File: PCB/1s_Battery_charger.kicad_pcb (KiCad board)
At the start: 2 copper layers, 40 x 57 mm, 54 parts, among them J1 Battery connector, J2 USB_C_Receptacle_PowerOnly_6P, J3 Battery connector, J4 Conn_01x04, J5 Battery connector, J6 Conn_01x03, U1 TCA9548APWR, U2 BQ25895RTW, U3 XIAO-ESP32-S3-SMD, U4 BQ25895RTW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

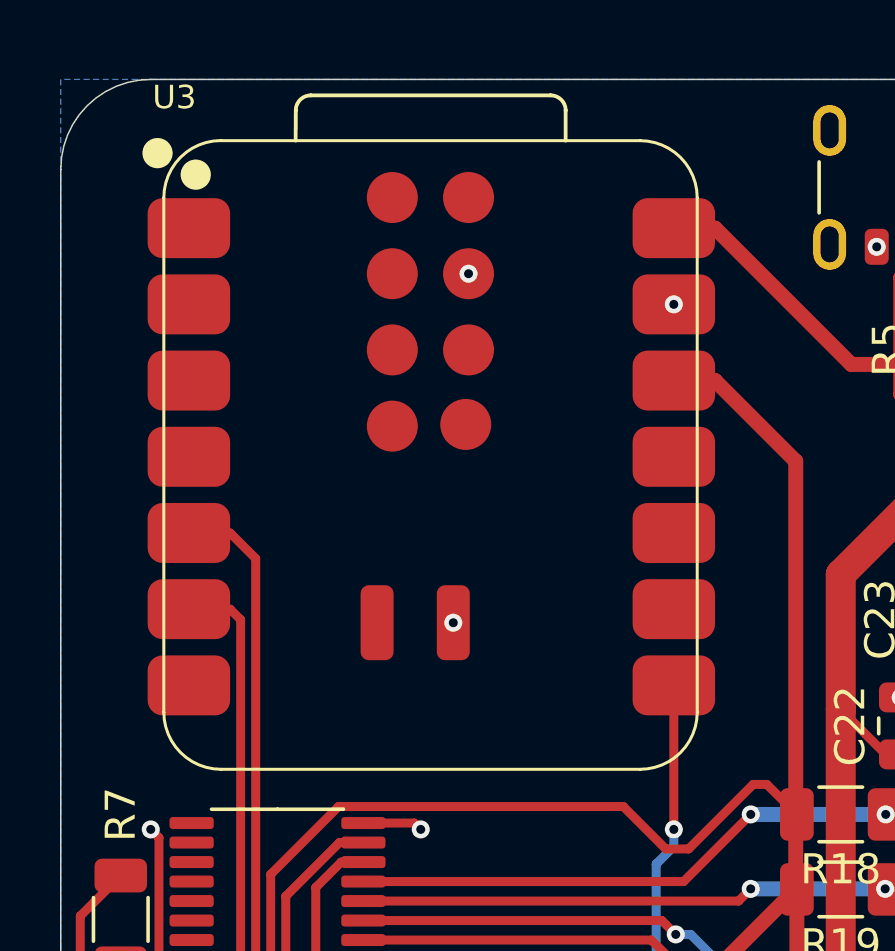
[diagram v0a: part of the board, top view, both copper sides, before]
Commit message: Fixed the issue with XIAO module being too far from the board edge
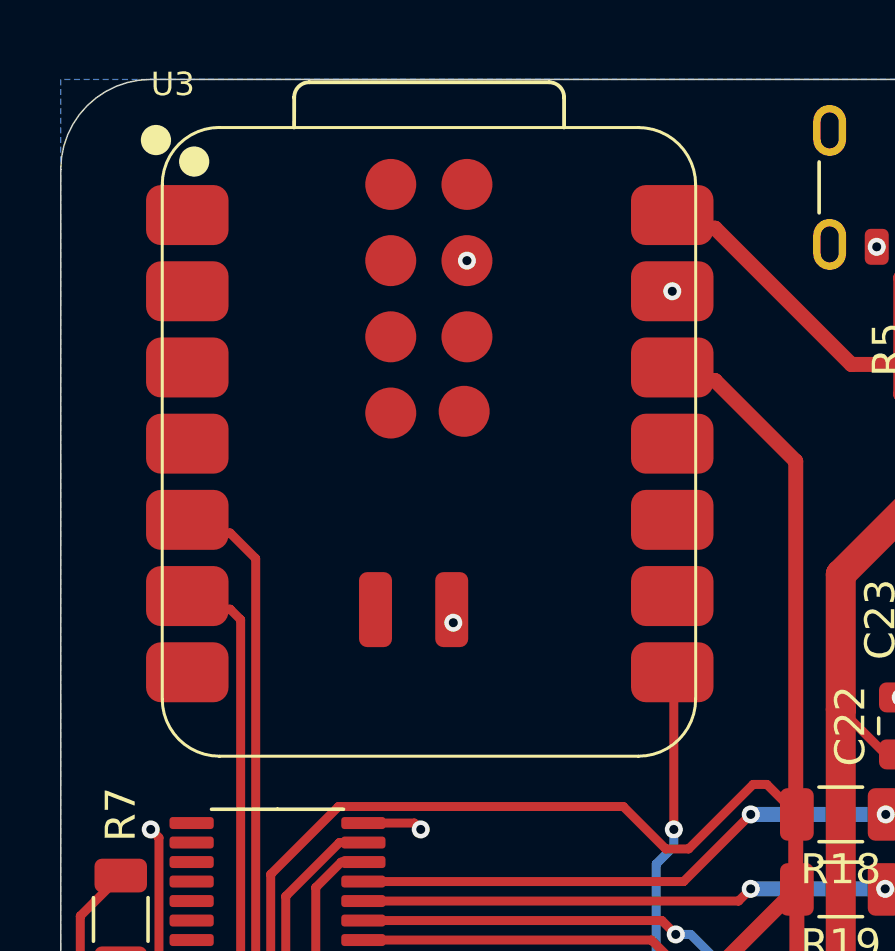
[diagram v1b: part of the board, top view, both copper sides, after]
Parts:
- moved U3 0.44 mm to (64.5, 26.6)
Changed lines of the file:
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@@
 	(footprint "Custom:XIAO-ESP32C6-SMD"
 		(layer "F.Cu")
-		(at 64.5526 27.0568)
+		(at 64.5 26.62)
 		(property "Reference" "U3"
 			(at -9.5 -11.5 0)
@@
 	)
 	(via
+		(at 72.3834 21.5615)
+		(size 0.6)
+		(drill 0.3)
+		(layers "F.Cu" "B.Cu")
+		(net 1)
+	)
+	(via
 		(at 62.5875 51.5)
 		(size 0.6)
@@
 	)
 	(via
-		(at 72.436 21.9983)
-		(size 0.6)
-		(drill 0.3)
-		(layers "F.Cu" "B.Cu")
-		(net 1)
-	)
-	(via
 		(at 64 39.5)
 		(size 0.6)
@@
 	)
 	(via
-		(at 65.5926 20.9768)
+		(at 84.7 20.08)
 		(size 0.6)
 		(drill 0.3)
@@
 	)
 	(via
-		(at 84.7 20.08)
+		(at 65.54 20.54)
 		(size 0.6)
 		(drill 0.3)
